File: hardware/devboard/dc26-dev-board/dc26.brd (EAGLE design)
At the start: 126 x 70 mm, 102 parts, among them CN1 JST, IC3 LDL112D33R, J1 DC26 Shitty AddOn, J2 DC26 Shitty AddOn, P1 SSSS811101, Y1 ABL-8.000MHZ-B2

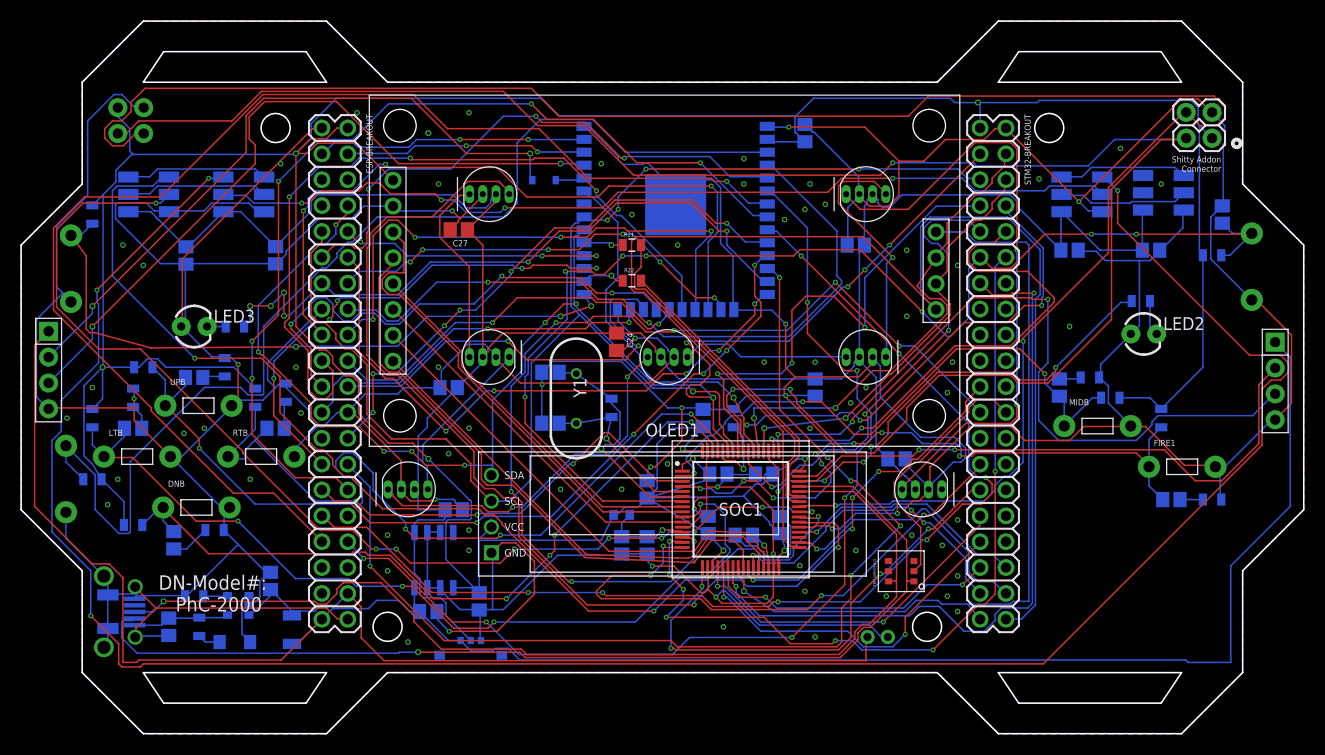
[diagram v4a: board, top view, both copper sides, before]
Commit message: increased the size of the apa106f5 wholes updated ratsnet
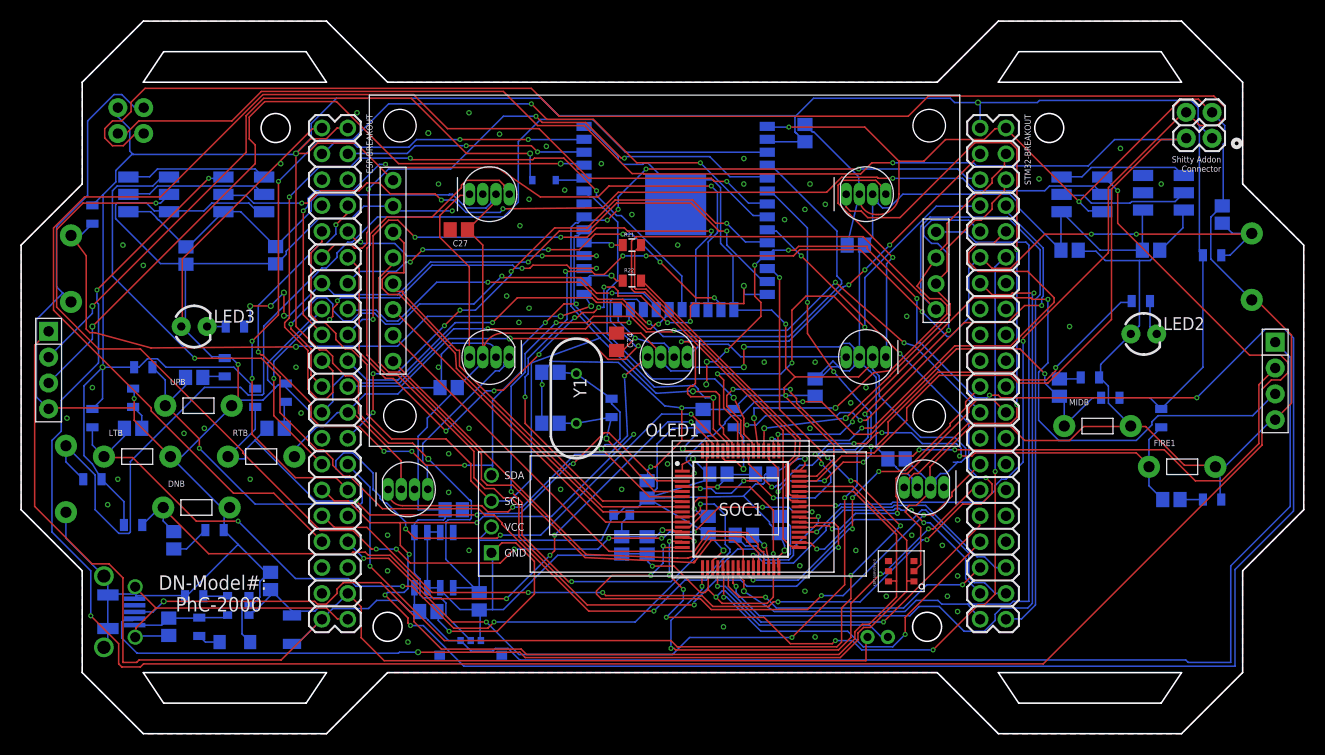
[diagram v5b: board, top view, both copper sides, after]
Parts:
- moved 106-7 0.28 mm to (90.7, 24.2)
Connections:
- removed net SIMPLE_LED2: SOC1.35
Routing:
- net IO26: track 59.8 -> 246.9 mm, vias 5 -> 13
- net GND: track 835.6 -> 805.1 mm, vias 80 -> 83
- net VIN-EN: track 214.6 -> 226.5 mm, vias 0 -> 2
- net IO12: track 59.3 -> 66.7 mm, vias 5 -> 9
- net N$17: track 61.2 -> 62.3 mm
- net IO34: track 101.2 -> 100.1 mm
- net LCD_DATA_CMD: track 38.3 -> 39.0 mm
- net ESP_I2C_SCL: track 137.1 -> 137.7 mm

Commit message: Added art work, fixed via drills, and started some initial trace cleanup.  Still need to move Cmdc0de/Krux logos into place.
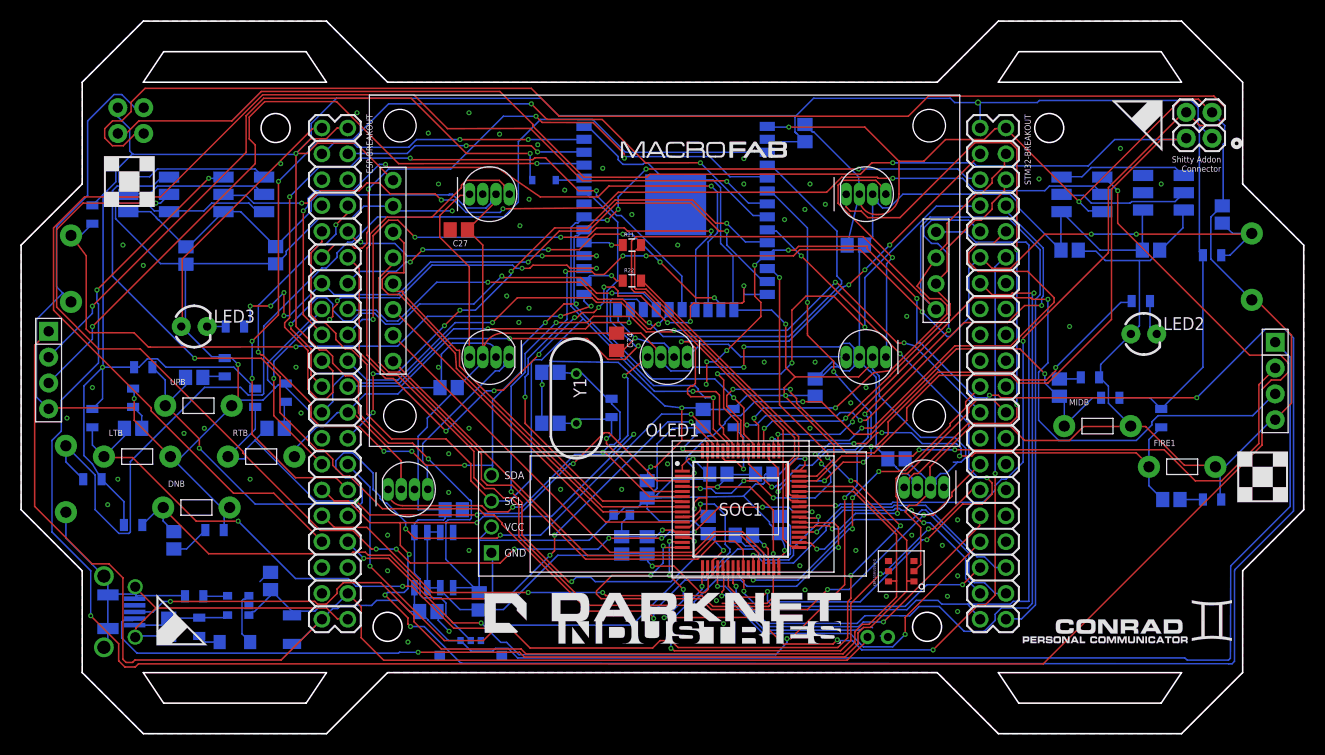
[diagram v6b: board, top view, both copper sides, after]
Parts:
- added U$10, U$11, U$9: FIDUCIAL_DNCORNER, darknet_parts_library:FIDUCIAL_CORNER
- added U$12: MACROFAB_LOGO, darknet_parts_library:MACROFAB_LOGO
- added U$3: DC26_KRUX_PUZZLE_1, darknet_parts_library:DN26_KRUX_PUZZLE_1
- added U$4: DC26_KRUX_PUZZLE_2, darknet_parts_library:DN26_KRUX_PUZZLE_2
- added U$5: CONRAD_LOGO, darknet_parts_library:CONRAD_LOGO
- added U$6: DN_LOGODC26, darknet_parts_library:DN_LOGO_DC26
- added U$7, U$8: FIDUCIAL_DNBOX, darknet_parts_library:FIDUCIAL_BOX
- U$1: value CMD_C0DE_LOGO -> KRUX_LOGO; device dc-26:CMD_C0DE_LOGO -> darknet_parts_library:KRUX_LOGO
- U$2: value KRUX_LOGO -> CMD_C0DE_LOGO; device dc-26:KRUX_LOGO -> darknet_parts_library:CMD_C0DE_LOGO
- moved U$2 113.8 mm to (0.92, 55.6)
- moved U$1 44.1 mm to (131.3, 53.0)
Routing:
- net GND: track 805.1 -> 761.5 mm
- net VCC: track 392.9 -> 395.0 mm
- net IO27: track 105.7 -> 107.5 mm
- net VCC1: track 70.9 -> 69.8 mm
- net GPIO_APA102_DATA: track 107.5 -> 108.6 mm
- net PA6: track 29.1 -> 29.9 mm
- net VIN: track 192.8 -> 192.1 mm
- net OSC_IN: track 17.1 -> 17.8 mm
- net PA7: track 71.9 -> 72.5 mm
- net LCD_RESET: track 59.6 -> 59.0 mm
- net ESP-IO0: track 65.0 -> 65.6 mm
- net PA0: track 95.5 -> 96.1 mm
- net PA1: track 79.8 -> 80.4 mm
- net IO12: track 66.7 -> 66.1 mm
- net IO34: track 100.1 -> 100.6 mm
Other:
- board text removed: "DN-Model#: PhC-2000"
- board text removed: "Personal Hyperwave Communicator"
